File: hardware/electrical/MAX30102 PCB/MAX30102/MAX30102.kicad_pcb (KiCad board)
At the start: 2 copper layers, 39.4 x 17.8 mm, 3 parts, among them J1 Conn_01x04, J2 Conn_01x04, J3 Conn_01x04

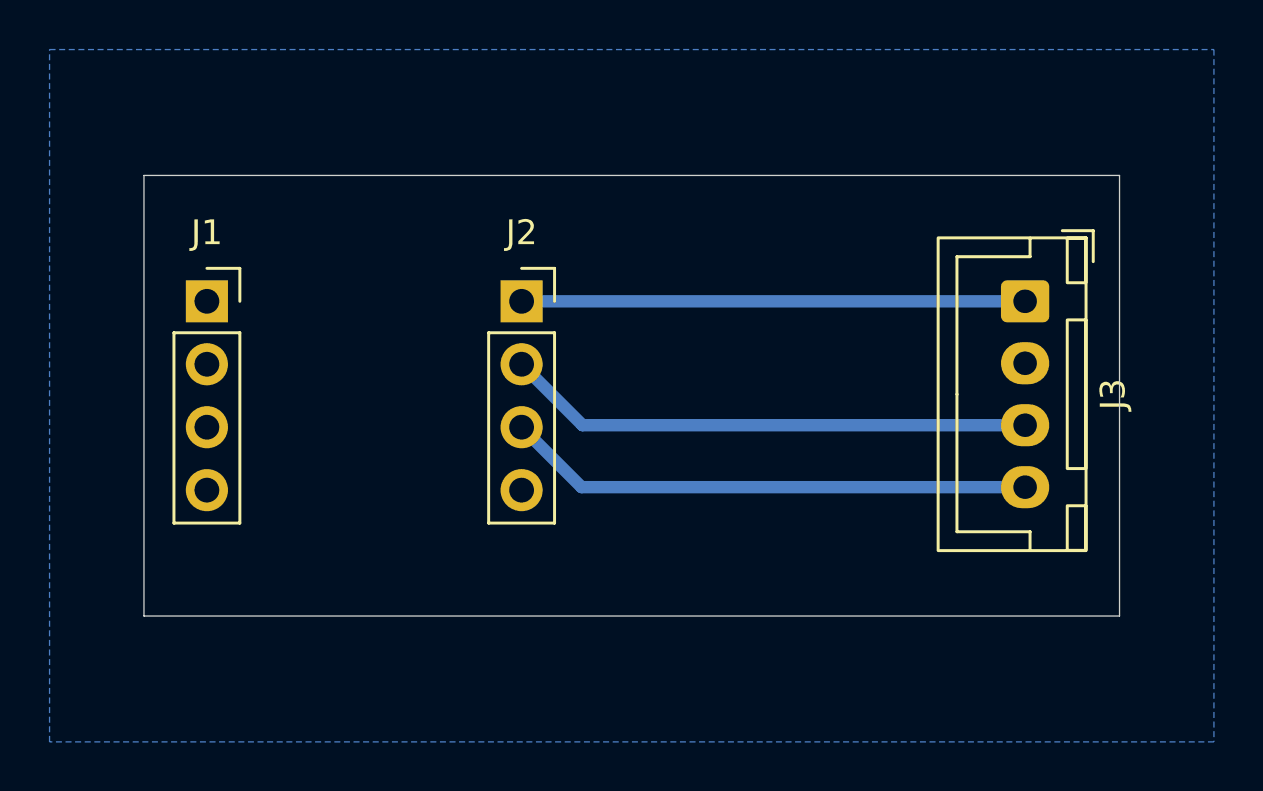
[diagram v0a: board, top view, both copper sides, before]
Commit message: backup sensor and limit switch PCBs
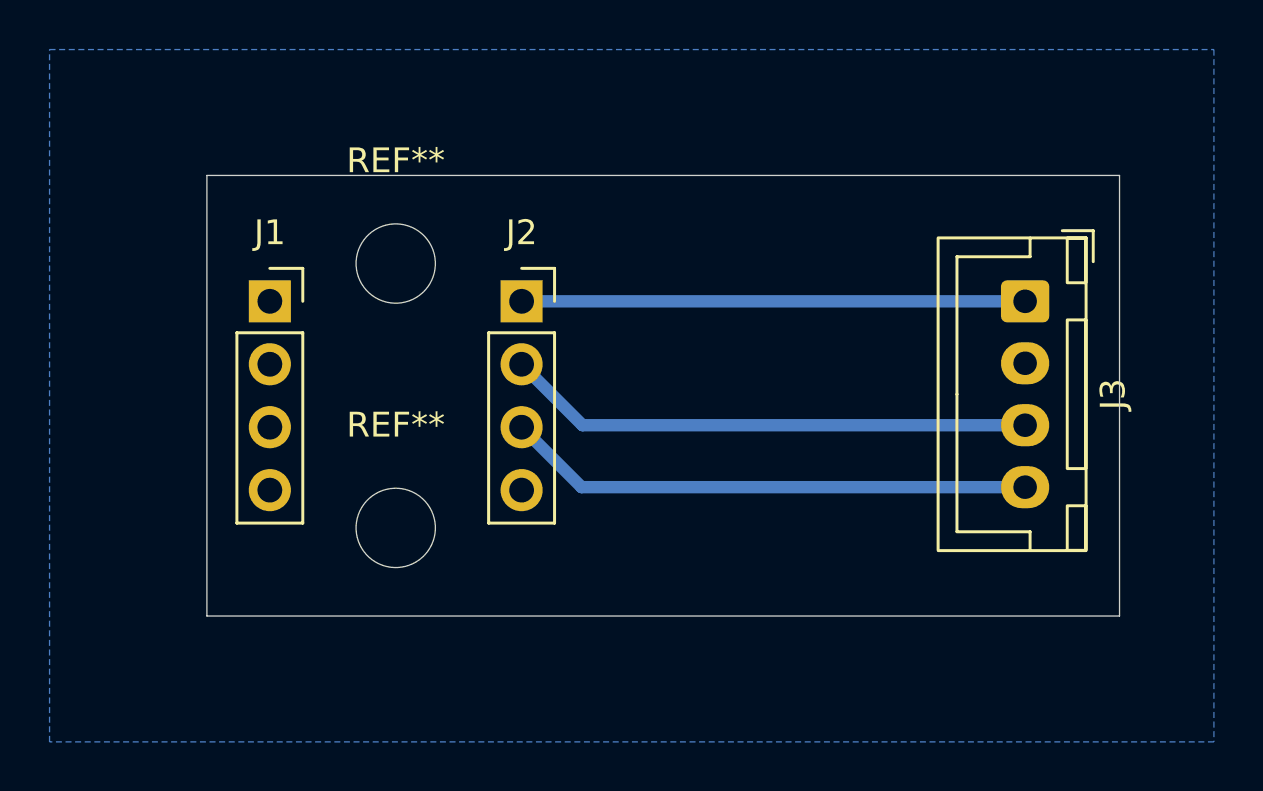
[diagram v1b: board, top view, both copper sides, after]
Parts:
- added REF**: MountingHole_3.2mm_M3, MountingHole:MountingHole_3.2mm_M3, F.Cu at (119.4, 92.5)
- added REF**: MountingHole_3.2mm_M3, MountingHole:MountingHole_3.2mm_M3, F.Cu at (119.4, 103.1)
- moved J1 2.54 mm to (114.3, 94.0)
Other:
- board size 39.4 x 17.8 mm -> 36.8 x 17.8 mm
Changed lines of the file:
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@@
 		(filling no)
 		(pcbplotparams
-			(layerselection 0x00000000_00000000_55555555_5755f5ff)
+			(layerselection 0x00000000_00000000_55555555_5755555f)
 			(plot_on_all_layers_selection 0x00000000_00000000_00000000_00000000)
 			(disableapertmacros no)
 			(usegerberextensions no)
-			(usegerberattributes yes)
-			(usegerberadvancedattributes yes)
+			(usegerberattributes no)
+			(usegerberadvancedattributes no)
 			(creategerberjobfile yes)
 			(dashed_line_dash_ratio 12)
@@
 			(outputformat 1)
 			(mirror no)
-			(drillshape 1)
+			(drillshape 0)
 			(scaleselection 1)
-			(outputdirectory "")
-		)
+			(outputdirectory "gerbers/")
+		)
+	)
+	(footprint "MountingHole:MountingHole_3.2mm_M3"
+		(layer "F.Cu")
+		(at 119.38 92.456)
+		(descr "Mounting Hole 3.2mm, M3, no annular, generated by kicad-footprint-generator mountinghole.py")
+		(tags "mountinghole M3")
+		(property "Reference" "REF**"
+			(at 0 -4.15 0)
+			(layer "F.SilkS")
+			(effects
+				(font
+					(size 1 1)
+					(thickness 0.15)
+				)
+			)
+		)
+		(property "Value" "MountingHole_3.2mm_M3"
+			(at 0 4.15 0)
+			(layer "F.Fab")
+			(effects
+				(font
+					(size 1 1)
+					(thickness 0.15)
+				)
+			)
+		)
+		(property "Datasheet" ""
+			(at 0 0 0)
+			(layer "F.Fab")
+			(hide yes)
+			(effects
+				(font
+					(size 1.27 1.27)
+				)
+			)
+		)
+		(property "Description" ""
+			(at 0 0 0)
+			(layer "F.Fab")
+			(hide yes)
+			(effects
+				(font
+					(size 1.27 1.27)
+				)
+			)
+		)
+		(property "KiLib_Generator" "mounting_hardware/mounting_hole"
+			(at 0 0 0)
+			(layer "F.SilkS")
+			(hide yes)
+			(effects
+				(font
+					(size 1 1)
+					(thickness 0.15)
+				)
+			)
+		)
+		(attr exclude_from_pos_files exclude_from_bom)
+		(duplicate_pad_numbers_are_jumpers no)
+		(fp_circle
+			(center 0 0)
+			(end 3.2 0)
+			(stroke
+				(width 0.15)
+				(type solid)
+			)
+			(fill no)
+			(layer "Cmts.User")
+		)
+		(fp_circle
+			(center 0 0)
+			(end 3.45 0)
+			(stroke
+				(width 0.05)
+				(type solid)
+			)
+			(fill no)
+			(layer "F.CrtYd")
+		)
+		(fp_text user "${REFERENCE}"
+			(at 0 0 0)
+			(layer "F.Fab")
+			(effects
+				(font
+					(size 1 1)
+					(thickness 0.15)
+				)
+			)
+		)
+		(pad "" np_thru_hole circle
+			(at 0 0)
+			(size 3.2 3.2)
+			(drill 3.2)
+			(layers "*.Cu" "*.Mask")
+		)
+		(embedded_fonts no)
 	)
 	(footprint "Connector_PinSocket_2.54mm:PinSocket_1x04_P2.54mm_Vertical"
 		(layer "F.Cu")
-		(at 111.76 93.98)
+		(at 114.3 93.98)
 		(descr "Through hole straight socket strip, 1x04, 2.54mm pitch, single row (from Kicad 4.0.7), script generated")
 		(tags "Through hole socket strip THT 1x04 2.54mm single row")
@@
 		)
 	)
+	(footprint "MountingHole:MountingHole_3.2mm_M3"
+		(layer "F.Cu")
+		(at 119.38 103.124)
+		(descr "Mounting Hole 3.2mm, M3, no annular, generated by kicad-footprint-generator mountinghole.py")
+		(tags "mountinghole M3")
+		(property "Reference" "REF**"
+			(at 0 -4.15 0)
+			(layer "F.SilkS")
+			(effects
+				(font
+					(size 1 1)
+					(thickness 0.15)
+				)
+			)
+		)
+		(property "Value" "MountingHole_3.2mm_M3"
+			(at 0 4.15 0)
+			(layer "F.Fab")
+			(effects
+				(font
+					(size 1 1)
+					(thickness 0.15)
+				)
+			)
+		)
+		(property "Datasheet" ""
+			(at 0 0 0)
+			(layer "F.Fab")
+			(hide yes)
+			(effects
+				(font
+					(size 1.27 1.27)
+				)
+			)
+		)
+		(property "Description" ""
+			(at 0 0 0)
+			(layer "F.Fab")
+			(hide yes)
+			(effects
+				(font
+					(size 1.27 1.27)
+				)
+			)
+		)
+		(property "KiLib_Generator" "mounting_hardware/mounting_hole"
+			(at 0 0 0)
+			(layer "F.SilkS")
+			(hide yes)
+			(effects
+				(font
+					(size 1 1)
+					(thickness 0.15)
+				)
+			)
+		)
+		(attr exclude_from_pos_files exclude_from_bom)
+		(duplicate_pad_numbers_are_jumpers no)
+		(fp_circle
+			(center 0 0)
+			(end 3.2 0)
+			(stroke
+				(width 0.15)
+				(type solid)
+			)
+			(fill no)
+			(layer "Cmts.User")
+		)
+		(fp_circle
+			(center 0 0)
+			(end 3.45 0)
+			(stroke
+				(width 0.05)
+				(type solid)
+			)
+			(fill no)
+			(layer "F.CrtYd")
+		)
+		(fp_text user "${REFERENCE}"
+			(at 0 0 0)
+			(layer "F.Fab")
+			(effects
+				(font
+					(size 1 1)
+					(thickness 0.15)
+				)
+			)
+		)
+		(pad "" np_thru_hole circle
+			(at 0 0)
+			(size 3.2 3.2)
+			(drill 3.2)
+			(layers "*.Cu" "*.Mask")
+		)
+		(embedded_fonts no)
+	)
 	(footprint "Connector_PinSocket_2.54mm:PinSocket_1x04_P2.54mm_Vertical"
 		(layer "F.Cu")
@@
 	)
 	(gr_rect
-		(start 109.22 88.9)
+		(start 111.76 88.9)
 		(end 148.59 106.68)
 		(radius 2)
@@
 		(fill no)
 		(layer "Edge.Cuts")
+	)
+	(segment
+		(start 144.78 93.98)
+		(end 124.46 93.98)
+		(width 0.5)
+		(layer "B.Cu")
+		(net "/VIN")
 	)
 	(segment
@@
 		(net "/SCL")
 	)
-	(segment
-		(start 144.78 93.98)
-		(end 124.46 93.98)
-		(width 0.5)
-		(layer "B.Cu")
-		(net "/VIN")
-	)
 	(zone
